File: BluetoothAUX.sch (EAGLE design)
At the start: 15 parts, among them IC2 TPA6132A2, J3 AUDIO_JACK_TRRSSMD_RA, J4 USB

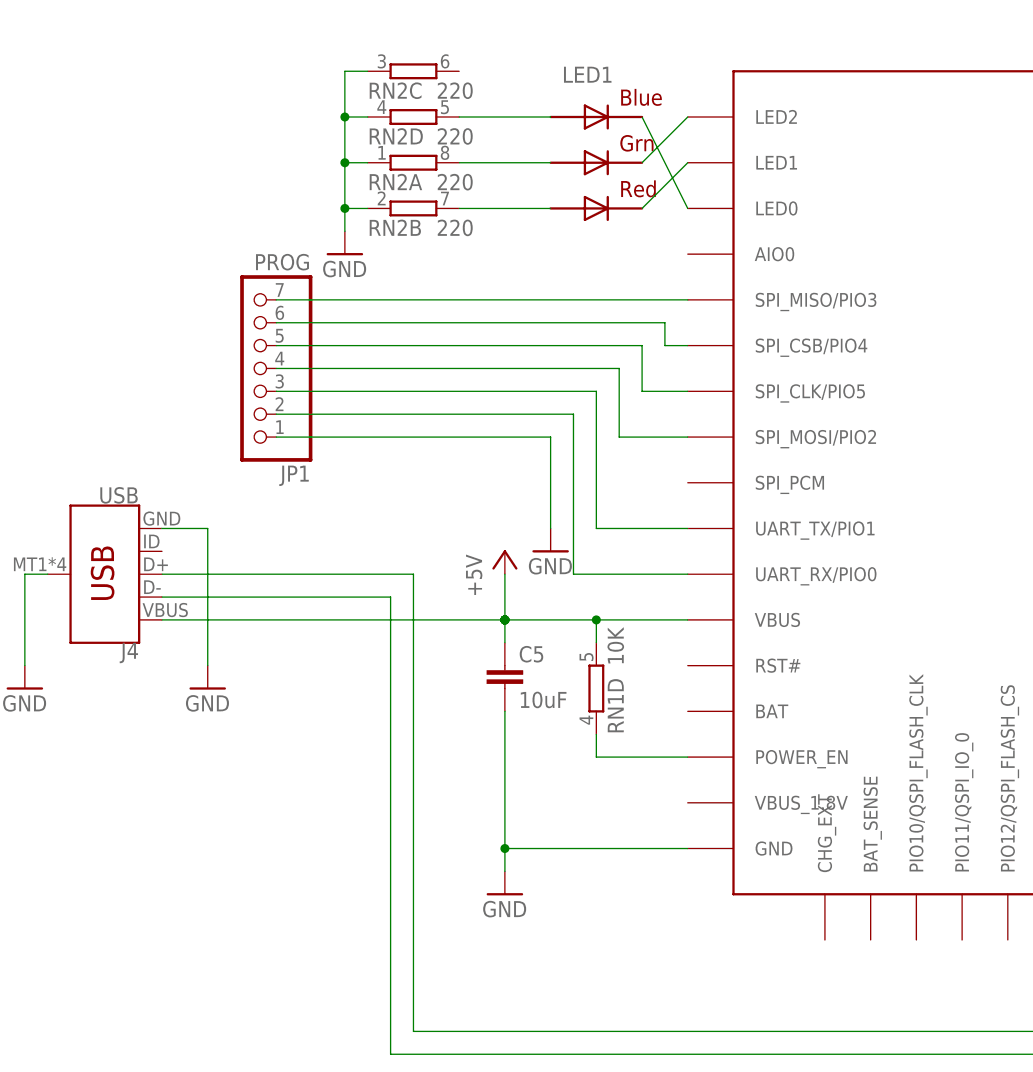
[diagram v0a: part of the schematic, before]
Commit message: VBAT_SENSE, POWER_EN, LEDs
Connect VBAT_SENSE to BAT
Delay on POWER_EN
Swap LED colors
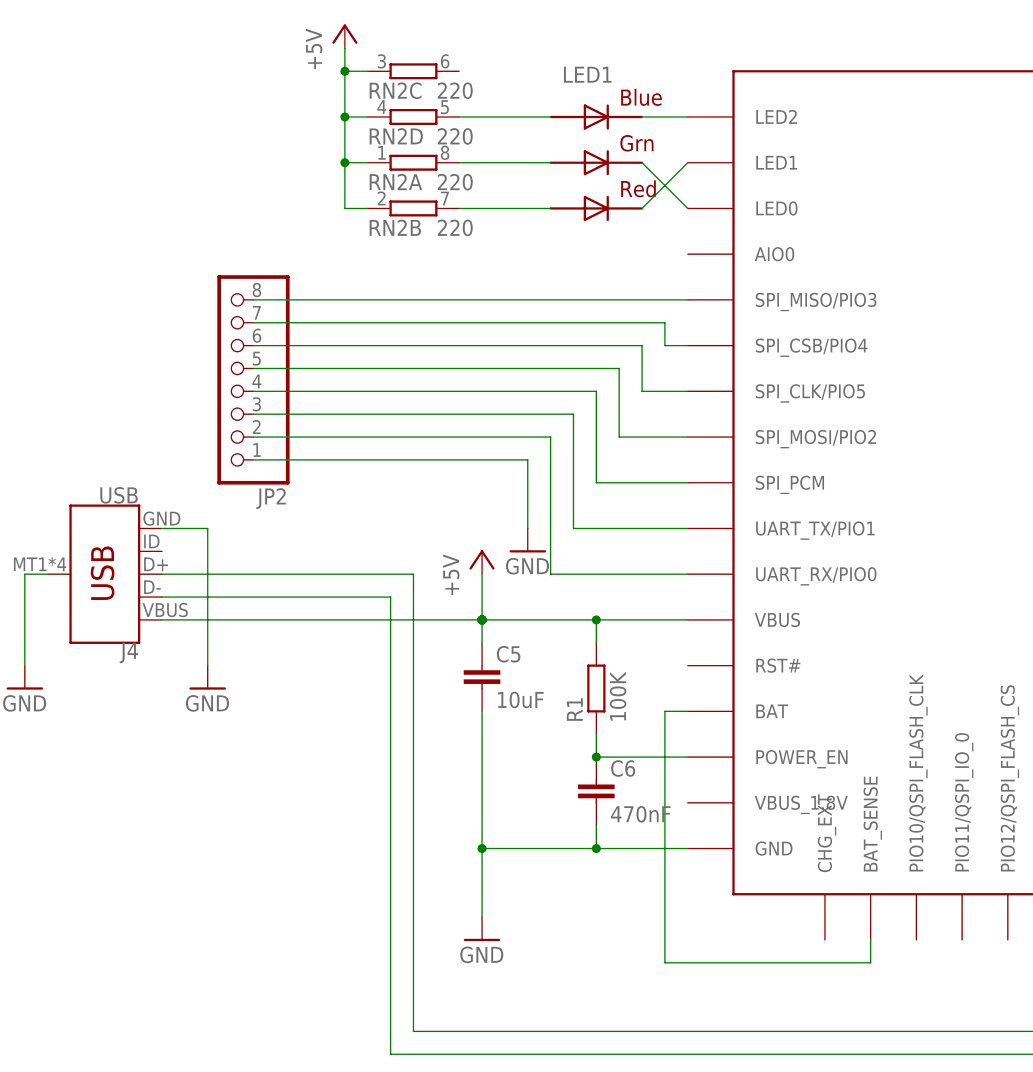
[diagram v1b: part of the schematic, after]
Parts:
- removed JP1: PROG, pinhead:PINHD-1X7
- added C6: 470nF, resistor:C-EUC0603
- added JP2: (no value), pinhead:PINHD-1X8
- added R1: 100K, resistor:R-EU_R0603
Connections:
- net LED1 renamed N$3
- removed net LED0: LED1.BLUE_C, U$1.LED0
- removed net LED2: LED1.GREEN_C, U$1.LED2
- new net N$1: JP2.4, U$1.SPI_PCM
- new net N$2: LED1.GREEN_C, U$1.LED0
- new net N$4: LED1.BLUE_C, U$1.LED2
- new net N$5: U$1.BAT, U$1.BAT_SENSE
- net +5V: now also R1.2, RN2A.1, RN2B.1, RN2C.1, RN2D.1; no longer RN1D.2
- net CLK: now also JP2.6; no longer JP1.5
- net CS: now also JP2.7; no longer JP1.6
- net GND: now also C6.2, JP2.1; no longer JP1.1, RN2A.1, RN2B.1, RN2C.1, RN2D.1
- net MISO: now also JP2.8; no longer JP1.7
- net MOSI: now also JP2.5; no longer JP1.4
- net POWER_EN: now also C6.1, R1.1; no longer RN1D.1
- net RX: now also JP2.2; no longer JP1.2
- net TX: now also JP2.3; no longer JP1.3
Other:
- moved on the sheet: C5

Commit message: Route
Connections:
- net N$5 renamed VBAT_SENSE
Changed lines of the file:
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@@
 </segment>
 </net>
-<net name="N$5" class="0">
+<net name="VBAT_SENSE" class="0">
 <segment>
 <pinref part="U$1" gate="G$1" pin="BAT_SENSE"/>

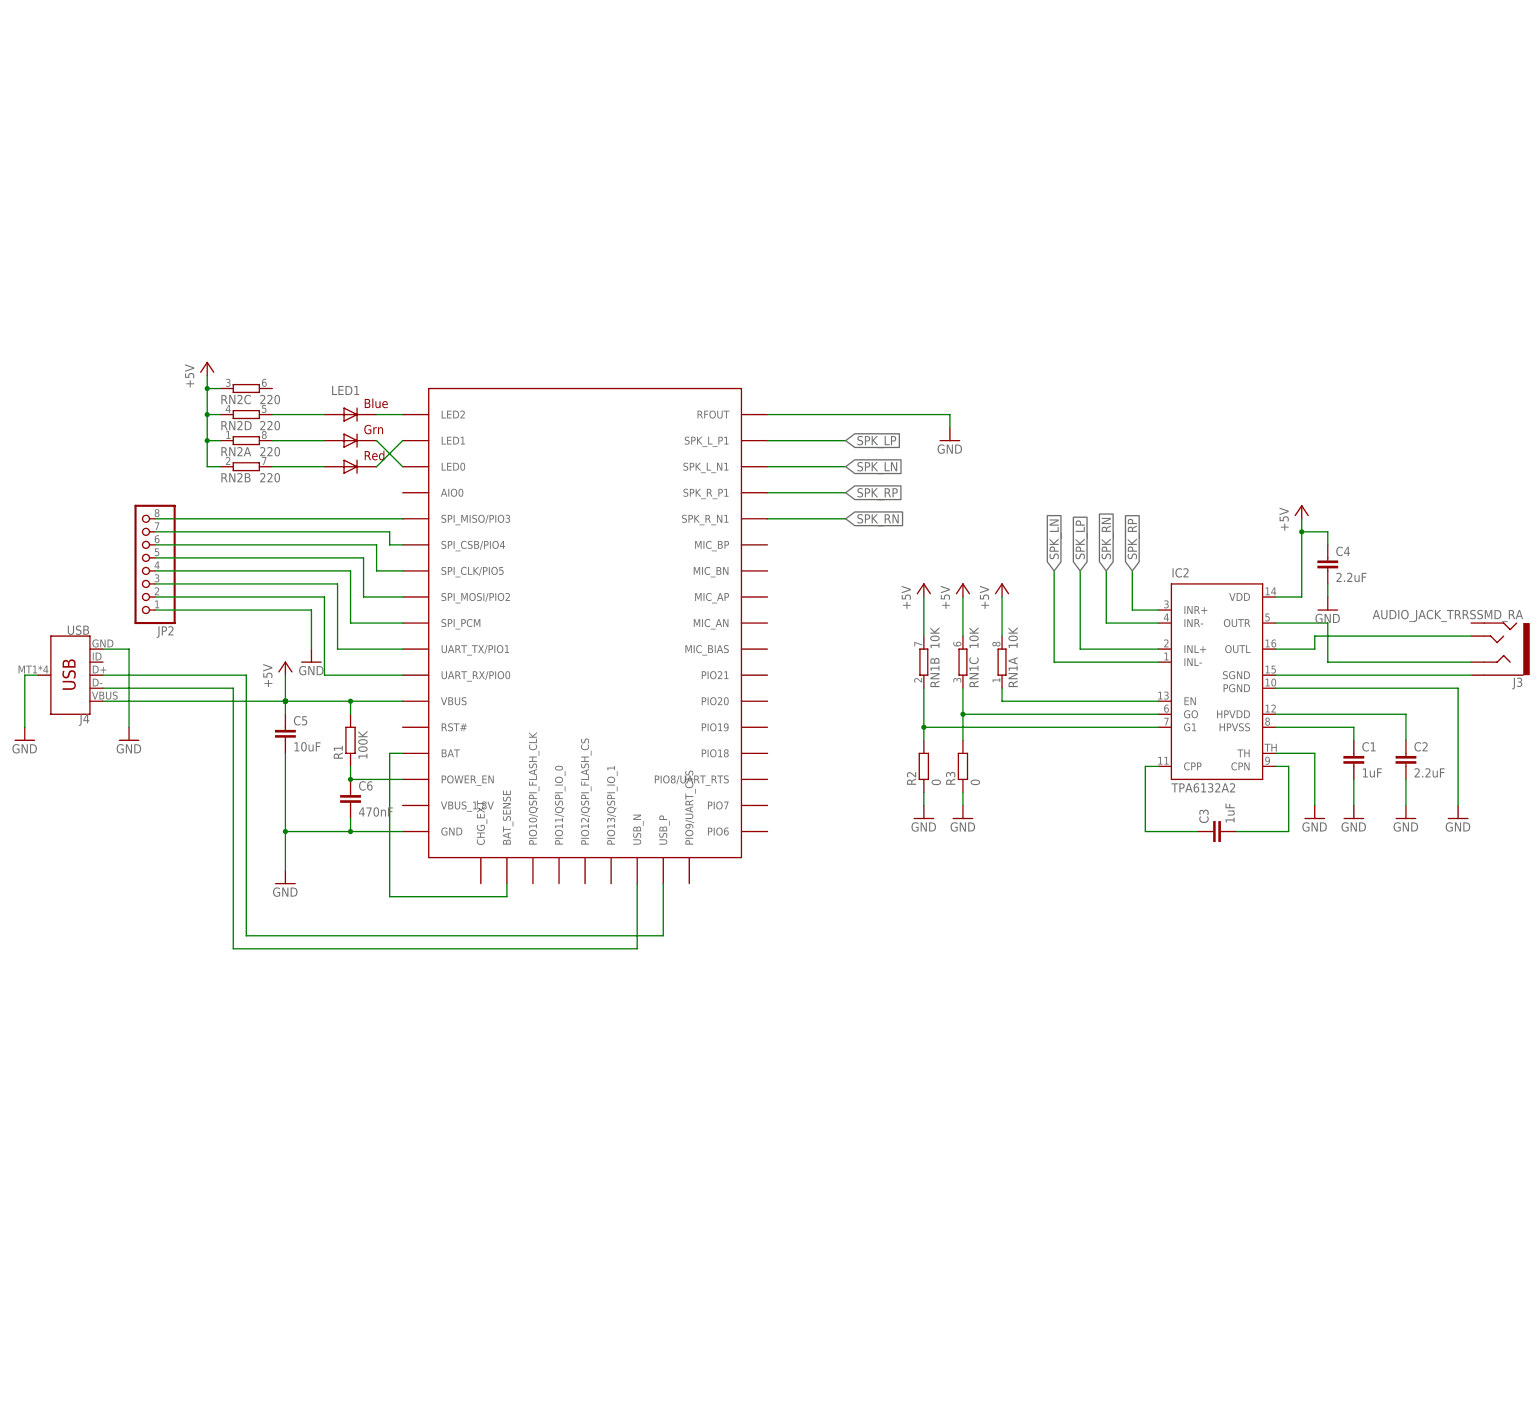
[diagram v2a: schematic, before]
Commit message: Delay circuit with MOSFET
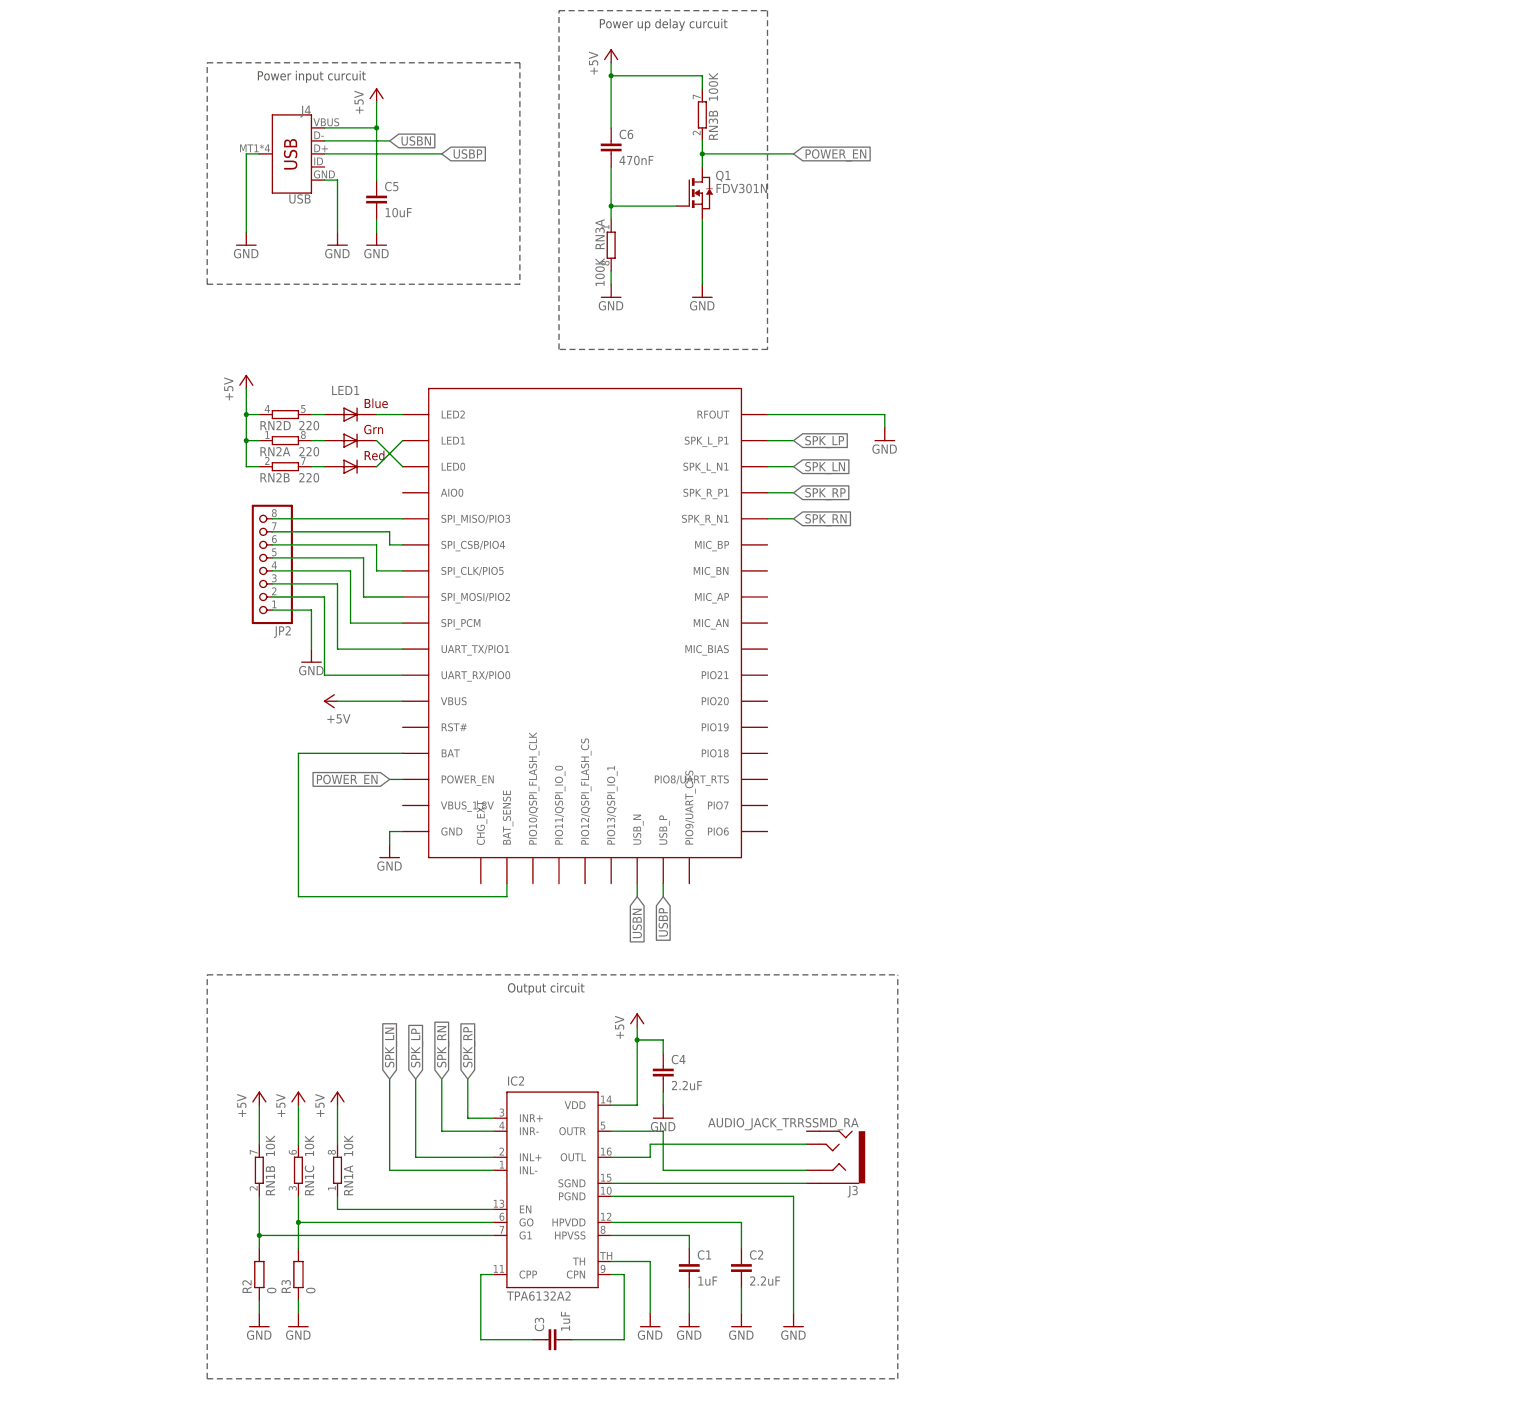
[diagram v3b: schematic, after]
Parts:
- removed R1: 100K, resistor:R-EU_R0603
- added Q1: FDV301N, FDV301N:FDV301N
- added RN3: 100K, resistor-dil:4R-N0603-ARC
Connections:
- new net N$5: C6.2, Q1.G, RN3A.1
- net +5V: now also C6.1, RN3B.2; no longer R1.2, RN2C.1
- net GND: now also Q1.S, RN3A.2; no longer C6.2
- net POWER_EN: now also Q1.D, RN3B.1; no longer C6.1, R1.1
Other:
- note added: "Output circuit"
- note added: "Power input curcuit"
- note added: "Power up delay curcuit"
- moved on the sheet: C1, C2, C3, C4, C5, C6, IC2, J3, J4, JP2, R2, R3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

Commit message: SPI_PCM resistor
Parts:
- added R1: 0, resistor:R-EU_R0603
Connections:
- new net SPI_PCM: JP2.4, R1.1
- net +5V: now also RN1D.2, RN2C.1
- net N$1: now also R1.2; no longer JP2.4
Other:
- moved on the sheet: JP2
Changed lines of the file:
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@@
 <part name="GND15" library="supply1" deviceset="GND" device=""/>
 <part name="P+8" library="supply1" deviceset="+5V" device=""/>
+<part name="P+9" library="supply1" deviceset="+5V" device=""/>
+<part name="R1" library="resistor" library_urn="urn:adsk.eagle:library:348" deviceset="R-EU_" device="R0603" package3d_urn="urn:adsk.eagle:package:26057/1" value="0"/>
 </parts>
 <sheets>
@@
 <instance part="GND5" gate="1" x="-38.1" y="40.64"/>
 <instance part="GND6" gate="1" x="-144.78" y="78.74"/>
-<instance part="GND7" gate="1" x="-149.86" y="-2.54"/>
+<instance part="GND7" gate="1" x="-160.02" y="-2.54"/>
 <instance part="GND3" gate="1" x="-134.62" y="-40.64"/>
 <instance part="P+3" gate="1" x="-147.32" y="-10.16" rot="R90"/>
@@
 <instance part="GND9" gate="1" x="-83.82" y="-132.08"/>
 <instance part="P+1" gate="1" x="-162.56" y="53.34"/>
-<instance part="JP2" gate="A" x="-160.02" y="17.78" rot="R180"/>
+<instance part="JP2" gate="A" x="-170.18" y="17.78" rot="R180"/>
 <instance part="C6" gate="G$1" x="-91.44" y="99.06"/>
 <instance part="GND2" gate="1" x="-91.44" y="68.58"/>
@@
 <instance part="GND15" gate="1" x="-137.16" y="78.74"/>
 <instance part="P+8" gate="1" x="-137.16" y="109.22"/>
+<instance part="RN1" gate="D" x="-30.48" y="-22.86"/>
+<instance part="RN2" gate="C" x="-30.48" y="-12.7"/>
+<instance part="P+9" gate="1" x="-45.72" y="-12.7" rot="R90"/>
+<instance part="R1" gate="G$1" x="-144.78" y="10.16" rot="R270"/>
 </instances>
 <busses>
@@
 <segment>
 <pinref part="GND7" gate="1" pin="GND"/>
-<wire x1="-149.86" y1="7.62" x2="-149.86" y2="0" width="0.1524" layer="91"/>
+<wire x1="-160.02" y1="7.62" x2="-160.02" y2="0" width="0.1524" layer="91"/>
 <pinref part="JP2" gate="A" pin="1"/>
-<wire x1="-157.48" y1="7.62" x2="-149.86" y2="7.62" width="0.1524" layer="91"/>
+<wire x1="-167.64" y1="7.62" x2="-160.02" y2="7.62" width="0.1524" layer="91"/>
 </segment>
 <segment>
@@
 <junction x="-137.16" y="101.6"/>
 </segment>
+<segment>
+<pinref part="P+9" gate="1" pin="+5V"/>
+<pinref part="RN2" gate="C" pin="1"/>
+<wire x1="-43.18" y1="-12.7" x2="-38.1" y2="-12.7" width="0.1524" layer="91"/>
+<pinref part="RN1" gate="D" pin="2"/>
+<wire x1="-38.1" y1="-12.7" x2="-35.56" y2="-12.7" width="0.1524" layer="91"/>
+<wire x1="-25.4" y1="-22.86" x2="-38.1" y2="-22.86" width="0.1524" layer="91"/>
+<wire x1="-38.1" y1="-22.86" x2="-38.1" y2="-12.7" width="0.1524" layer="91"/>
+<junction x="-38.1" y="-12.7"/>
+</segment>
 </net>
 <net name="MISO" class="0">
@@
 <pinref part="U$1" gate="G$1" pin="SPI_MISO/PIO3"/>
 <pinref part="JP2" gate="A" pin="8"/>
-<wire x1="-157.48" y1="25.4" x2="-132.08" y2="25.4" width="0.1524" layer="91"/>
+<wire x1="-167.64" y1="25.4" x2="-132.08" y2="25.4" width="0.1524" layer="91"/>
 </segment>
 </net>
@@
 <pinref part="U$1" gate="G$1" pin="SPI_CSB/PIO4"/>
 <wire x1="-132.08" y1="20.32" x2="-134.62" y2="20.32" width="0.1524" layer="91"/>
-<wire x1="-157.48" y1="22.86" x2="-134.62" y2="22.86" width="0.1524" layer="91"/>
+<wire x1="-167.64" y1="22.86" x2="-134.62" y2="22.86" width="0.1524" layer="91"/>
 <wire x1="-134.62" y1="22.86" x2="-134.62" y2="20.32" width="0.1524" layer="91"/>
 <pinref part="JP2" gate="A" pin="7"/>
@@
 <pinref part="U$1" gate="G$1" pin="SPI_CLK/PIO5"/>
 <wire x1="-137.16" y1="15.24" x2="-132.08" y2="15.24" width="0.1524" layer="91"/>
-<wire x1="-157.48" y1="20.32" x2="-137.16" y2="20.32" width="0.1524" layer="91"/>
+<wire x1="-167.64" y1="20.32" x2="-137.16" y2="20.32" width="0.1524" layer="91"/>
 <wire x1="-137.16" y1="20.32" x2="-137.16" y2="15.24" width="0.1524" layer="91"/>
 <pinref part="JP2" gate="A" pin="6"/>
@@
 <pinref part="U$1" gate="G$1" pin="SPI_MOSI/PIO2"/>
 <wire x1="-139.7" y1="10.16" x2="-132.08" y2="10.16" width="0.1524" layer="91"/>
-<wire x1="-157.48" y1="17.78" x2="-139.7" y2="17.78" width="0.1524" layer="91"/>
+<wire x1="-167.64" y1="17.78" x2="-139.7" y2="17.78" width="0.1524" layer="91"/>
 <wire x1="-139.7" y1="17.78" x2="-139.7" y2="10.16" width="0.1524" layer="91"/>
 <pinref part="JP2" gate="A" pin="5"/>
@@
 <segment>
 <pinref part="U$1" gate="G$1" pin="UART_TX/PIO1"/>
-<wire x1="-132.08" y1="0" x2="-144.78" y2="0" width="0.1524" layer="91"/>
-<wire x1="-144.78" y1="12.7" x2="-144.78" y2="0" width="0.1524" layer="91"/>
+<wire x1="-132.08" y1="0" x2="-152.4" y2="0" width="0.1524" layer="91"/>
+<wire x1="-152.4" y1="12.7" x2="-152.4" y2="0" width="0.1524" layer="91"/>
 <pinref part="JP2" gate="A" pin="3"/>
-<wire x1="-157.48" y1="12.7" x2="-144.78" y2="12.7" width="0.1524" layer="91"/>
+<wire x1="-167.64" y1="12.7" x2="-152.4" y2="12.7" width="0.1524" layer="91"/>
 </segment>
 </net>
@@
 <segment>
 <pinref part="U$1" gate="G$1" pin="UART_RX/PIO0"/>
-<wire x1="-132.08" y1="-5.08" x2="-147.32" y2="-5.08" width="0.1524" layer="91"/>
-<wire x1="-147.32" y1="10.16" x2="-147.32" y2="-5.08" width="0.1524" layer="91"/>
+<wire x1="-132.08" y1="-5.08" x2="-154.94" y2="-5.08" width="0.1524" layer="91"/>
+<wire x1="-154.94" y1="10.16" x2="-154.94" y2="-5.08" width="0.1524" layer="91"/>
 <pinref part="JP2" gate="A" pin="2"/>
-<wire x1="-157.48" y1="10.16" x2="-147.32" y2="10.16" width="0.1524" layer="91"/>
+<wire x1="-167.64" y1="10.16" x2="-154.94" y2="10.16" width="0.1524" layer="91"/>
 </segment>
 </net>
@@
 </segment>
 </net>
-<net name="N$1" class="0">
+<net name="SPI_PCM" class="0">
 <segment>
 <pinref part="JP2" gate="A" pin="4"/>
-<pinref part="U$1" gate="G$1" pin="SPI_PCM"/>
-<wire x1="-157.48" y1="15.24" x2="-142.24" y2="15.24" width="0.1524" layer="91"/>
-<wire x1="-142.24" y1="15.24" x2="-142.24" y2="5.08" width="0.1524" layer="91"/>
-<wire x1="-142.24" y1="5.08" x2="-132.08" y2="5.08" width="0.1524" layer="91"/>
+<wire x1="-167.64" y1="15.24" x2="-144.78" y2="15.24" width="0.1524" layer="91"/>
+<pinref part="R1" gate="G$1" pin="1"/>
 </segment>
 </net>
@@
 </segment>
 </net>
+<net name="N$1" class="0">
+<segment>
+<pinref part="U$1" gate="G$1" pin="SPI_PCM"/>
+<pinref part="R1" gate="G$1" pin="2"/>
+<wire x1="-144.78" y1="5.08" x2="-132.08" y2="5.08" width="0.1524" layer="91"/>
+</segment>
+</net>
